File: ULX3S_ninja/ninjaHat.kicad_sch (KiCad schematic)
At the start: 14 parts, among them J1 DVI-HX-107DIP, P1 ULX3S connector (JP1)

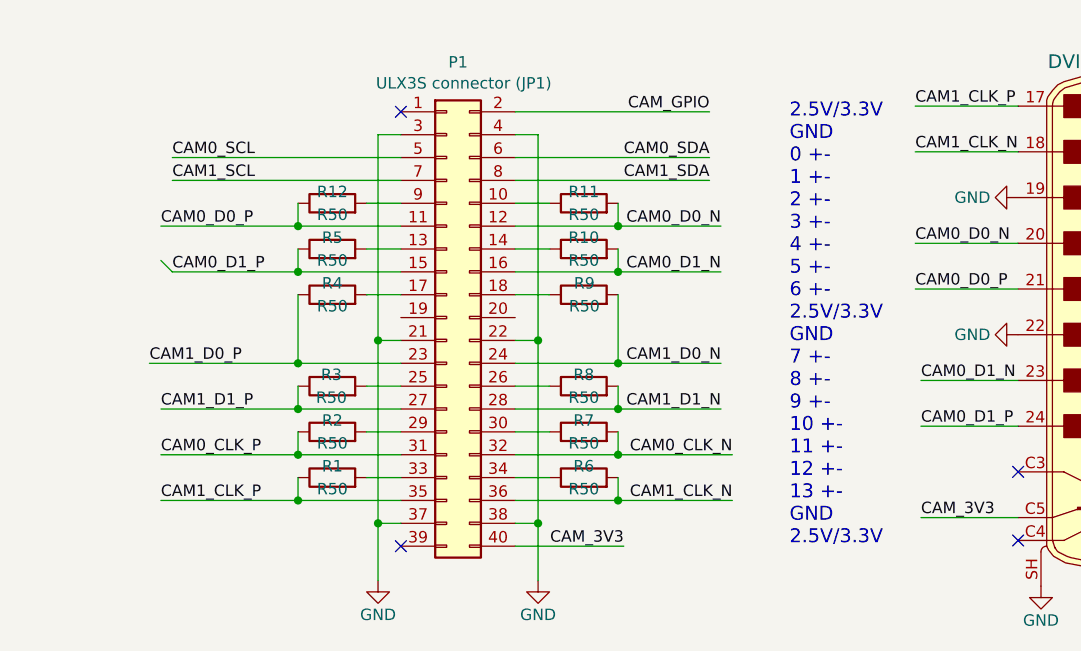
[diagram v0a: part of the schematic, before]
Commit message: small aesthetic change sin schematic; added schematic png
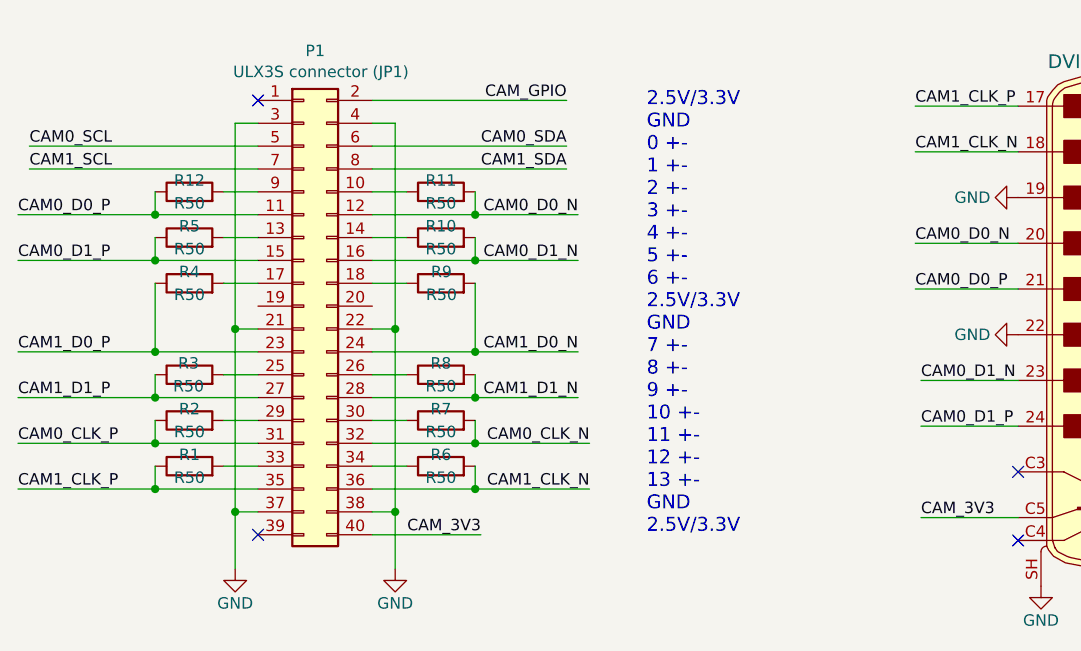
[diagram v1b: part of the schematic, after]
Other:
- moved on the sheet: P1, R1, R10, R11, R12, R2, R3, R4, R5, R6, R7, R8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

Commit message: Changed circuit
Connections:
- net CAM0_CLK_N: now also P1.34 (Pin_34), R10.2; no longer P1.32 (Pin_32), R7.2
- net CAM0_CLK_P: now also P1.33 (Pin_33), R5.1; no longer P1.31 (Pin_31), R2.1
- net CAM0_D0_N: now also P1.26 (Pin_26), R6.2; no longer P1.12 (Pin_12), R11.2
- net CAM0_D0_P: now also P1.25 (Pin_25), R1.1; no longer P1.11 (Pin_11), R12.1
- net CAM0_D1_N: now also P1.28 (Pin_28), R7.2; no longer P1.16 (Pin_16), R10.2
- net CAM0_D1_P: now also P1.27 (Pin_27), R2.1; no longer P1.15 (Pin_15), R5.1
- net CAM1_CLK_N: now also R11.2; no longer R6.2
- net CAM1_CLK_P: now also R12.1; no longer R1.1
- net CAM1_D0_N: now also P1.30 (Pin_30), R8.2; no longer P1.24 (Pin_24), R9.2
- net CAM1_D0_P: now also P1.29 (Pin_29), R3.1; no longer P1.23 (Pin_23), R4.1
- net CAM1_D1_N: now also P1.32 (Pin_32), R9.2; no longer P1.28 (Pin_28), R8.2
- net CAM1_D1_P: now also P1.31 (Pin_31), R4.1; no longer P1.27 (Pin_27), R3.1
- net at R5.2: now also P1.11 (Pin_11); no longer P1.13 (Pin_13)
- net at R10.1: now also P1.12 (Pin_12); no longer P1.14 (Pin_14)
- net at R4.2: now also P1.13 (Pin_13); no longer P1.17 (Pin_17)
- net at R9.1: now also P1.14 (Pin_14); no longer P1.18 (Pin_18)
- net at R3.2: now also P1.15 (Pin_15); no longer P1.25 (Pin_25)
- net at R8.1: now also P1.16 (Pin_16); no longer P1.26 (Pin_26)
- net at R2.2: now also P1.17 (Pin_17); no longer P1.29 (Pin_29)
- net at R7.1: now also P1.18 (Pin_18); no longer P1.30 (Pin_30)
- net at R1.2: now also P1.23 (Pin_23); no longer P1.33 (Pin_33)
- net at R6.1: now also P1.24 (Pin_24); no longer P1.34 (Pin_34)
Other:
- moved on the sheet: P1, R1, R10, R11, R12, R2, R3, R4, R5, R6, R7, R8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

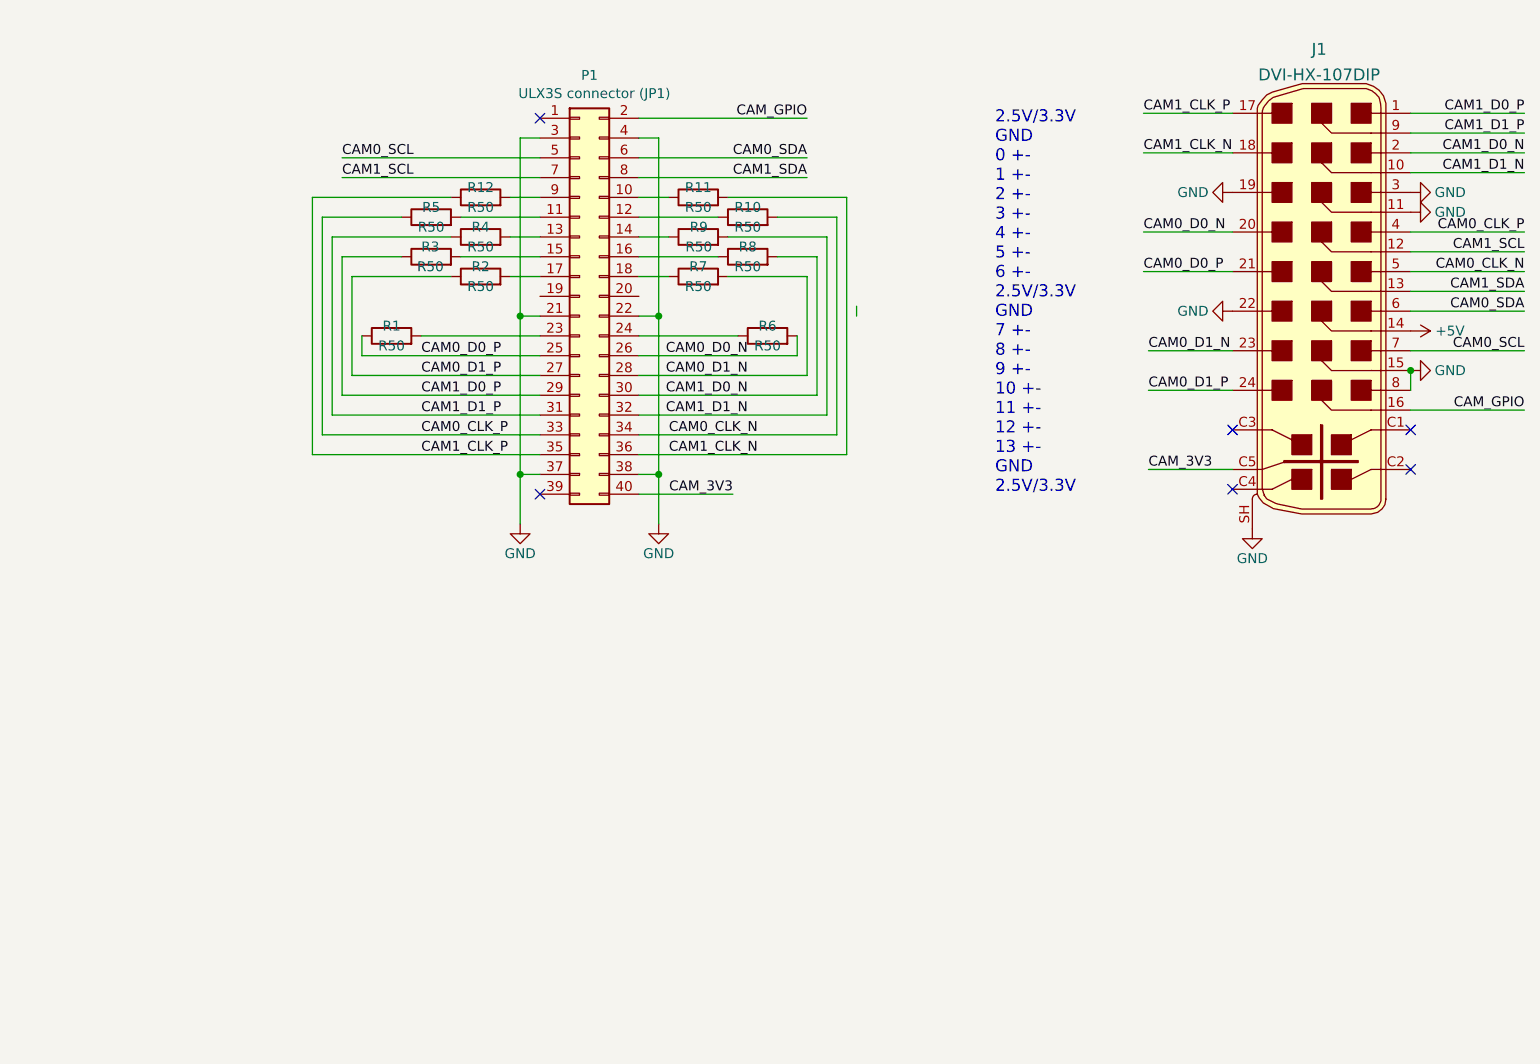
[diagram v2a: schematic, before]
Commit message: PCB work and pin mapping changed
Did a first PCB layout
changed the pin mapping towards FPGAs four easier routing, schematic need to be rechecked!
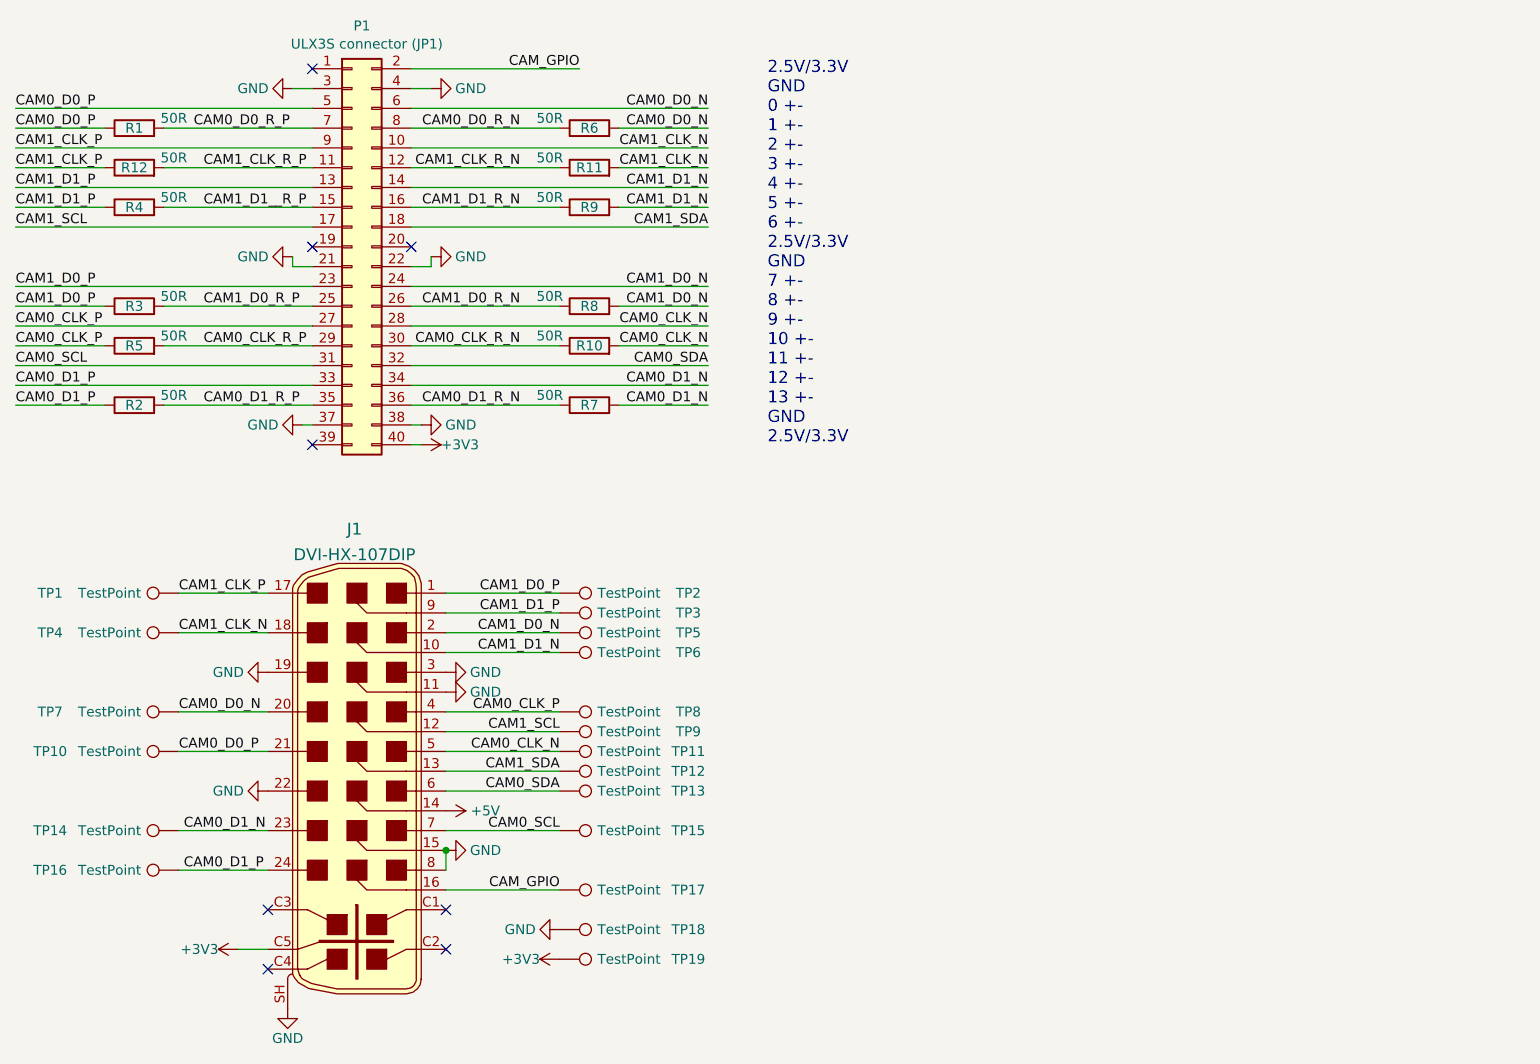
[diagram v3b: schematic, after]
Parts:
- added TP1, TP10, TP11, TP12, TP13, TP14, TP15, TP16, TP17, TP18, TP19, TP2, TP3, TP4, TP5, TP6, TP7, TP8, TP9: TestPoint, TestPoint:TestPoint_Pad_D1.5mm, symbol Connector:TestPoint
- R1, R10, R11, R12, R2, R3, R4, R5, R6, R7, R8, R9: value R50 -> 50R; footprint (none) -> Resistor_SMD:R_0805_2012Metric
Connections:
- net CAM0_CLK_N: now also P1.28 (Pin_28), TP11.1; no longer P1.34 (Pin_34)
- net CAM0_CLK_P: now also P1.27 (Pin_27), TP8.1; no longer P1.33 (Pin_33)
- net CAM0_D0_N: now also P1.6 (Pin_6), TP7.1; no longer P1.26 (Pin_26)
- net CAM0_D0_P: now also P1.5 (Pin_5), TP10.1; no longer P1.25 (Pin_25)
- net CAM0_D1_N: now also P1.34 (Pin_34), TP14.1; no longer P1.28 (Pin_28)
- net CAM0_D1_P: now also P1.33 (Pin_33), TP16.1; no longer P1.27 (Pin_27)
- net CAM0_SCL: now also P1.31 (Pin_31), TP15.1; no longer P1.5 (Pin_5)
- net CAM0_SDA: now also P1.32 (Pin_32), TP13.1; no longer P1.6 (Pin_6)
- net CAM1_CLK_N: now also P1.10 (Pin_10), TP4.1; no longer P1.36 (Pin_36)
- net CAM1_CLK_P: now also P1.9 (Pin_9), TP1.1; no longer P1.35 (Pin_35)
- net CAM1_D0_N: now also P1.24 (Pin_24), TP5.1; no longer P1.30 (Pin_30)
- net CAM1_D0_P: now also P1.23 (Pin_23), TP2.1; no longer P1.29 (Pin_29)
- net CAM1_D1_N: now also P1.14 (Pin_14), TP6.1; no longer P1.32 (Pin_32)
- net CAM1_D1_P: now also P1.13 (Pin_13), TP3.1; no longer P1.31 (Pin_31)
- net CAM1_SCL: now also P1.17 (Pin_17), TP9.1; no longer P1.7 (Pin_7)
- net CAM1_SDA: now also P1.18 (Pin_18), TP12.1; no longer P1.8 (Pin_8)
- net CAM_GPIO: now also TP17.1
- net GND: now also TP18.1
- net CAM1_CLK_R_N: now reaches R11.1
- net CAM1_CLK_R_N: now also P1.12 (Pin_12); no longer P1.10 (Pin_10)
- net CAM0_CLK_R_P: now reaches R5.2
- net CAM0_CLK_R_P: now also P1.29 (Pin_29); no longer P1.11 (Pin_11)
- net CAM0_CLK_R_N: now reaches R10.1
- net CAM0_CLK_R_N: now also P1.30 (Pin_30); no longer P1.12 (Pin_12)
- net CAM1_D1__R_P: now reaches R4.2
- net CAM1_D1__R_P: now also P1.15 (Pin_15); no longer P1.13 (Pin_13)
- net CAM1_D1_R_N: now reaches R9.1
- net CAM1_D1_R_N: now also P1.16 (Pin_16); no longer P1.14 (Pin_14)
- net CAM1_D0_R_P: now reaches R3.2
- net CAM1_D0_R_P: now also P1.25 (Pin_25); no longer P1.15 (Pin_15)
- net CAM1_D0_R_N: now reaches R8.1
- net CAM1_D0_R_N: now also P1.26 (Pin_26); no longer P1.16 (Pin_16)
- net CAM0_D1_R_P: now reaches R2.2
- net CAM0_D1_R_P: now also P1.35 (Pin_35); no longer P1.17 (Pin_17)
- net CAM0_D1_R_N: now reaches R7.1
- net CAM0_D1_R_N: now also P1.36 (Pin_36); no longer P1.18 (Pin_18)
- net CAM0_D0_R_P: now reaches R1.2
- net CAM0_D0_R_P: now also P1.7 (Pin_7); no longer P1.23 (Pin_23)
- net CAM0_D0_R_N: now reaches R6.1
- net CAM0_D0_R_N: now also P1.8 (Pin_8); no longer P1.24 (Pin_24)
- net CAM1_CLK_R_P: now reaches R12.2
- net CAM1_CLK_R_P: now also P1.11 (Pin_11); no longer P1.9 (Pin_9)
- net CAM_3V3 renamed +3V3
- net +3V3: now also TP19.1
- no-connect marks 6 -> 8
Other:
- moved on the sheet: J1, P1, R1, R10, R11, R12, R2, R3, R4, R5, R6, R7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

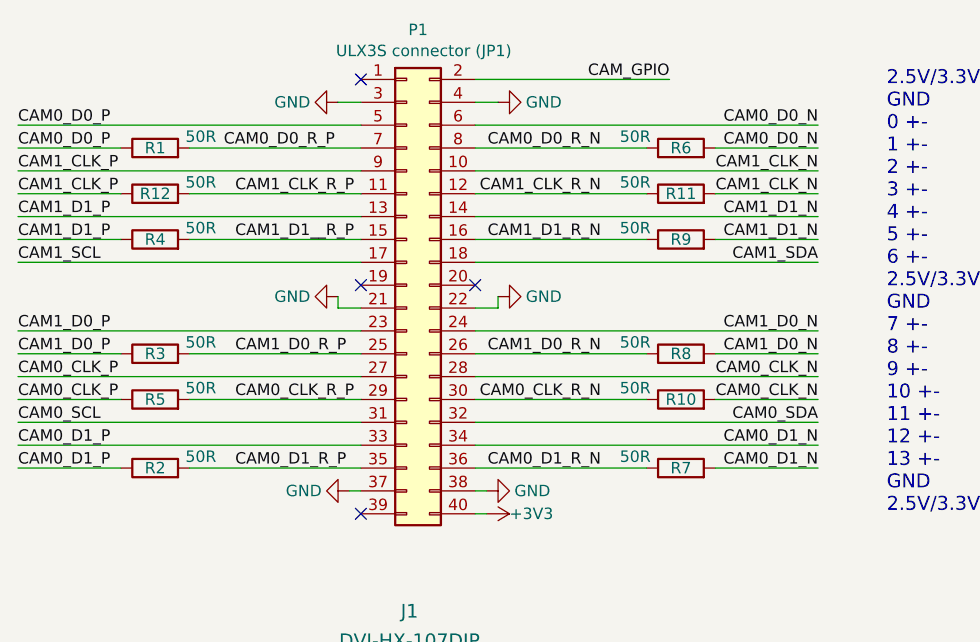
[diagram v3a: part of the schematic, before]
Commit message: Pin Mapping changed again
Please check
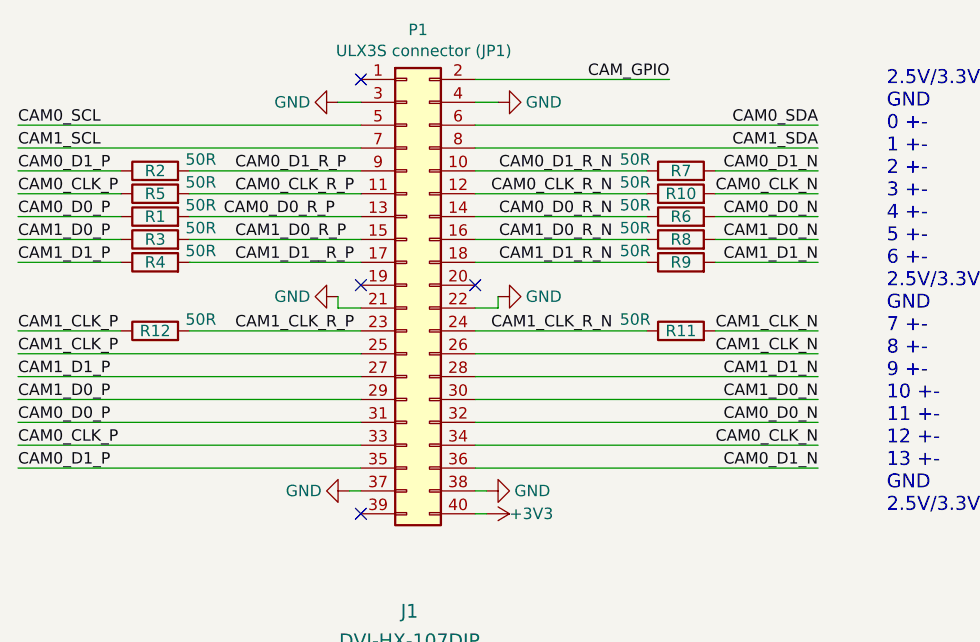
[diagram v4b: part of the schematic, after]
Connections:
- net CAM0_CLK_N: now also P1.34 (Pin_34); no longer P1.28 (Pin_28)
- net CAM0_CLK_P: now also P1.33 (Pin_33); no longer P1.27 (Pin_27)
- net CAM0_CLK_R_N: now also P1.12 (Pin_12); no longer P1.30 (Pin_30)
- net CAM0_CLK_R_P: now also P1.11 (Pin_11); no longer P1.29 (Pin_29)
- net CAM0_D0_N: now also P1.32 (Pin_32); no longer P1.6 (Pin_6)
- net CAM0_D0_P: now also P1.31 (Pin_31); no longer P1.5 (Pin_5)
- net CAM0_D0_R_N: now also P1.14 (Pin_14); no longer P1.8 (Pin_8)
- net CAM0_D0_R_P: now also P1.13 (Pin_13); no longer P1.7 (Pin_7)
- net CAM0_D1_N: now also P1.36 (Pin_36); no longer P1.34 (Pin_34)
- net CAM0_D1_P: now also P1.35 (Pin_35); no longer P1.33 (Pin_33)
- net CAM0_D1_R_N: now also P1.10 (Pin_10); no longer P1.36 (Pin_36)
- net CAM0_D1_R_P: now also P1.9 (Pin_9); no longer P1.35 (Pin_35)
- net CAM0_SCL: now also P1.5 (Pin_5); no longer P1.31 (Pin_31)
- net CAM0_SDA: now also P1.6 (Pin_6); no longer P1.32 (Pin_32)
- net CAM1_CLK_N: now also P1.26 (Pin_26); no longer P1.10 (Pin_10)
- net CAM1_CLK_P: now also P1.25 (Pin_25); no longer P1.9 (Pin_9)
- net CAM1_CLK_R_N: now also P1.24 (Pin_24); no longer P1.12 (Pin_12)
- net CAM1_CLK_R_P: now also P1.23 (Pin_23); no longer P1.11 (Pin_11)
- net CAM1_D0_N: now also P1.30 (Pin_30); no longer P1.24 (Pin_24)
- net CAM1_D0_P: now also P1.29 (Pin_29); no longer P1.23 (Pin_23)
- net CAM1_D0_R_N: now also P1.16 (Pin_16); no longer P1.26 (Pin_26)
- net CAM1_D0_R_P: now also P1.15 (Pin_15); no longer P1.25 (Pin_25)
- net CAM1_D1_N: now also P1.28 (Pin_28); no longer P1.14 (Pin_14)
- net CAM1_D1_P: now also P1.27 (Pin_27); no longer P1.13 (Pin_13)
- net CAM1_D1_R_N: now also P1.18 (Pin_18); no longer P1.16 (Pin_16)
- net CAM1_D1__R_P: now also P1.17 (Pin_17); no longer P1.15 (Pin_15)
- net CAM1_SCL: now also P1.7 (Pin_7); no longer P1.17 (Pin_17)
- net CAM1_SDA: now also P1.8 (Pin_8); no longer P1.18 (Pin_18)
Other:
- moved on the sheet: R1, R10, R11, R12, R2, R3, R4, R5, R6, R7, R8, R9
